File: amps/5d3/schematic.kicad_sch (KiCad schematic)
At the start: 43 parts, among them T2 PP : 8

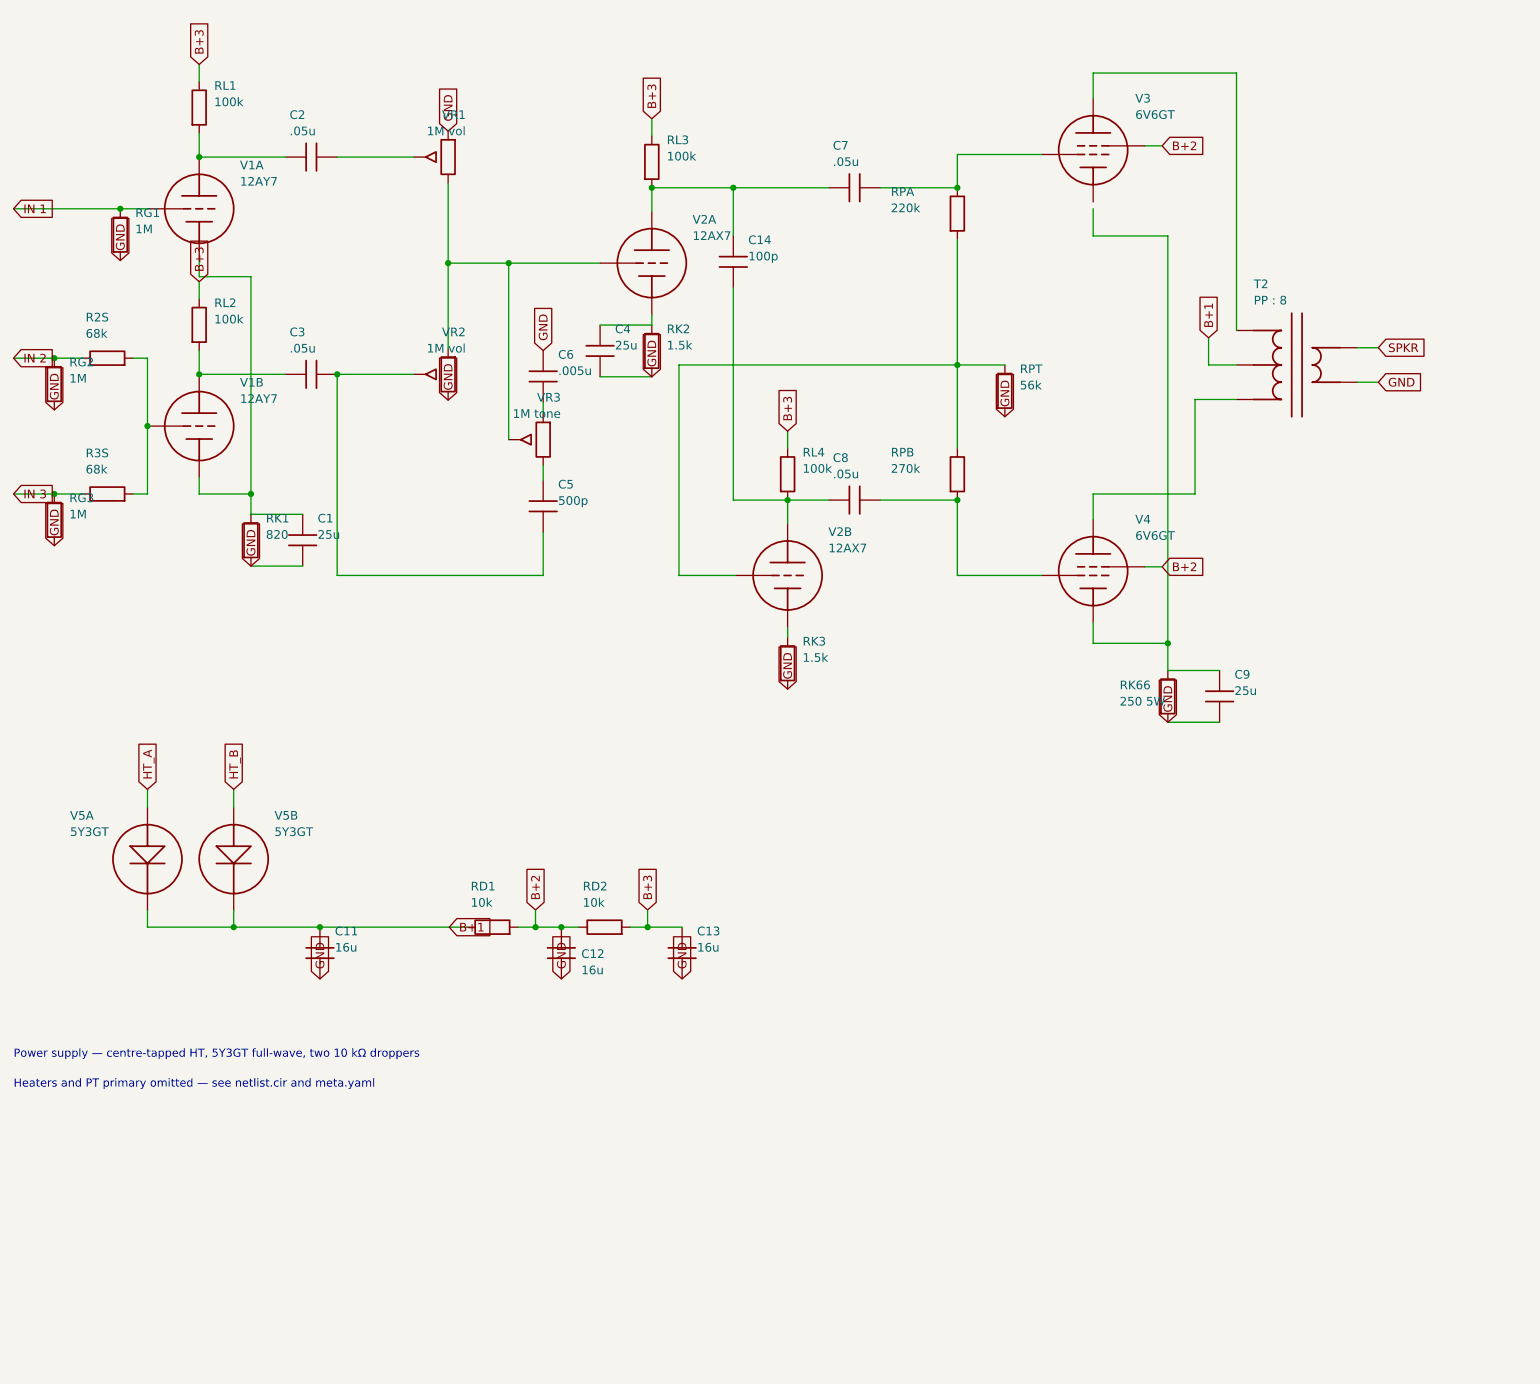
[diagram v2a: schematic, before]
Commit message: Fix: rotated global labels lettered their net names outside the flag
Every global label this pipeline emitted carried (justify left) regardless of
rotation. KiCanvas — like KiCad — draws label text horizontally at 0/180 and
vertically at 90/270 and reads WHICH SIDE of the anchor it letters on from the
justification, so at 180 and 270 the name printed outside an empty flag
outline, struck through by the very wire it names: 219 labels at 180 deg
(including the input-jack flags at top-left of nearly every sheet, the first
glyphs a visitor reads) and 792 GND/rail flags at 270 whose names squeezed at
the flag mouth instead of lettering down the body. The library already
compensated rotation for property text (`pa`); this mirrors that logic for
global labels: justify right at 180/270, left at 0/90.

check_schematics gains the geometry clause whose absence let all 1011
instances through a "no lettering through circuitry" pass: it modelled the
flag box but never the label TEXT, so a name rendered on the wrong side was
invisible to it. The gate now proves justification compensates rotation on
every global label.

Two more things this exposed, fixed in the same engine pass:

- Placement now measures with the renderer's own Newstroke advance table
  (extracted from the vendored kicanvas.js) instead of a flat 0.68-em prose
  average that under-read part lettering by a quarter — the mechanism behind
  every "metered clean, printed through its neighbour" incident. The GATE
  deliberately keeps the coarse ruler: re-ruling it with renderer truth was
  tried and red-flagged 28 of 34 sheets over abutments three visual passes
  had already judged sub-visual (the two-rulers note in schematic_lib.py).
- place_captions' escape ladder runs further, because a banner caption
  measured truly is half again wider than the old estimate believed.

All 34 schematics regenerated; full gate suite green.

🤖 Generated with [Claude Code](https://claude.com/claude-code)

Co-Authored-By: Claude Fable 5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
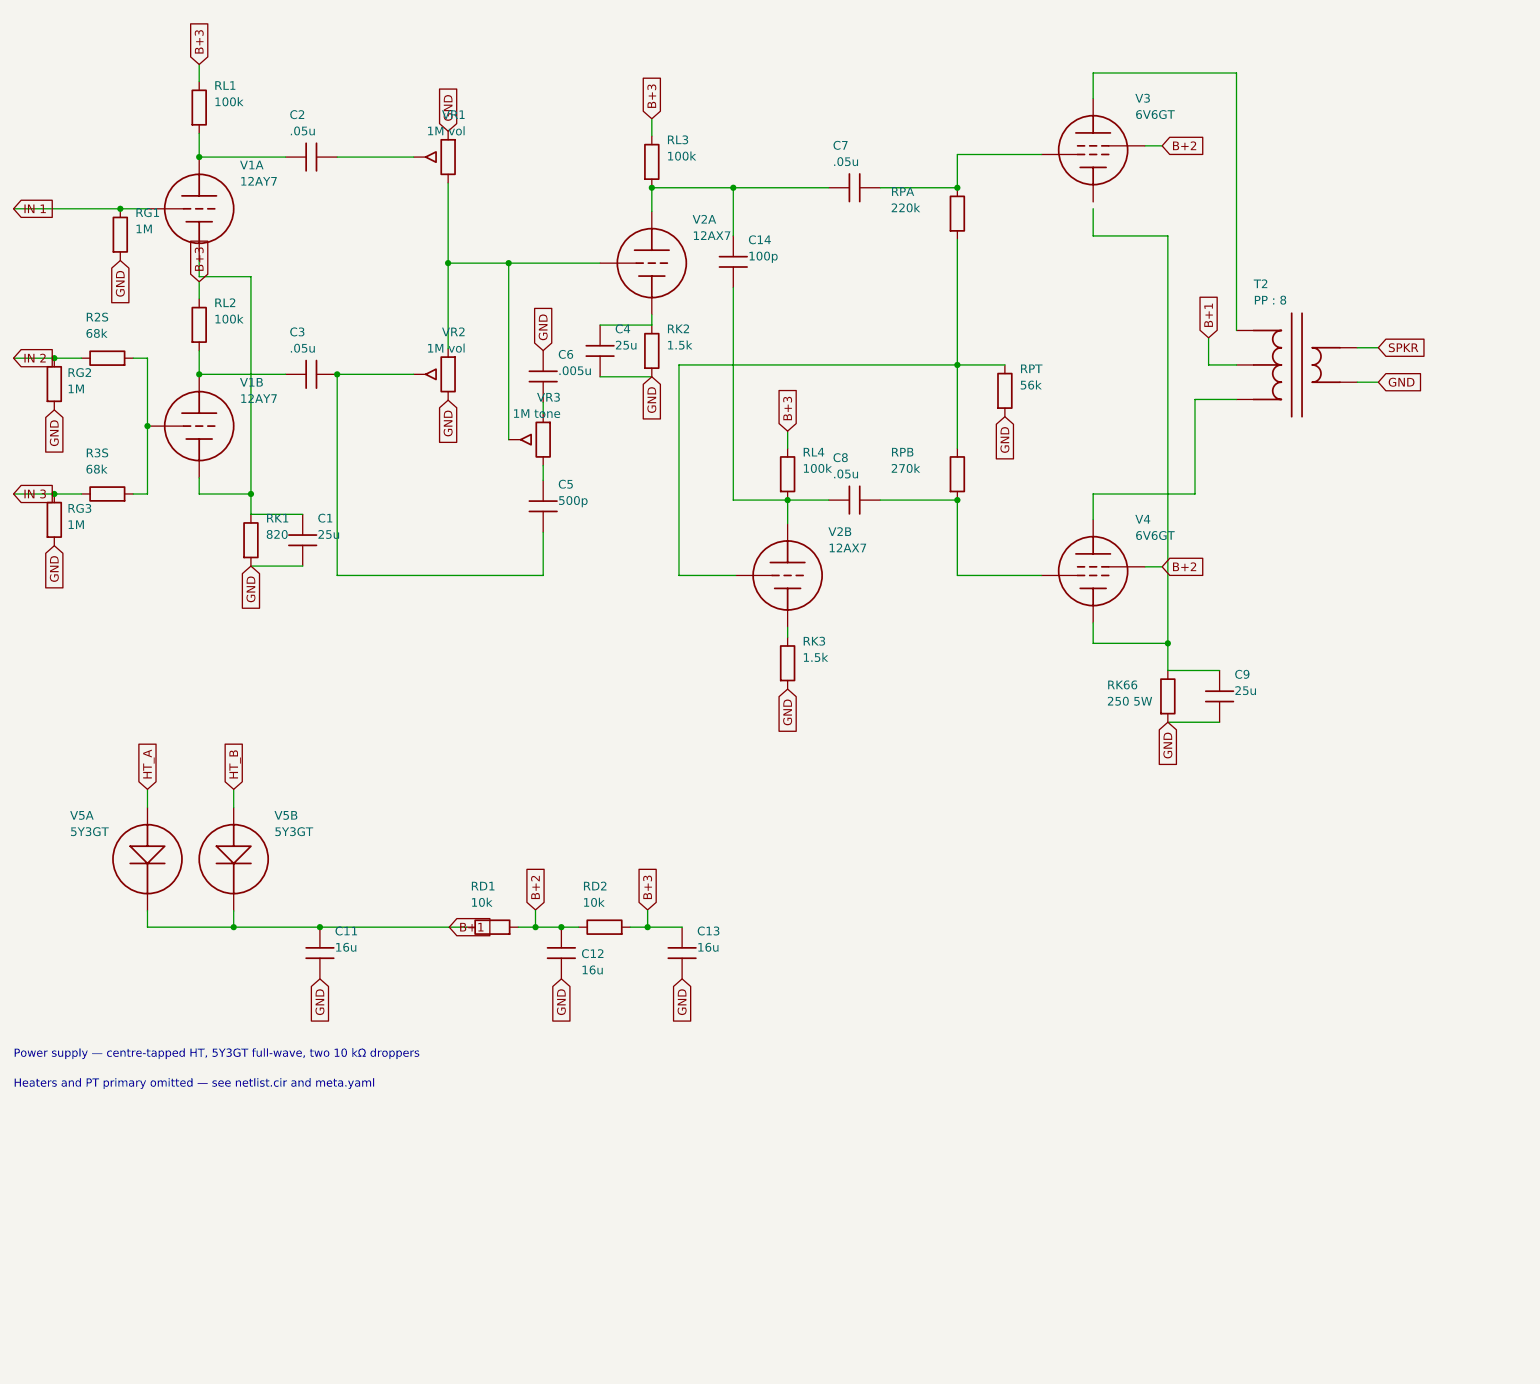
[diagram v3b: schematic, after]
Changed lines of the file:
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@@
     (property "Value" "1M" (at 30.62 41.288 0) (effects (font (size 1.27 1.27)) (justify left))))
   (global_label "GND" (shape input) (at 28.42 45.898 270)
-    (effects (font (size 1.27 1.27)) (justify left)))
+    (effects (font (size 1.27 1.27)) (justify right)))
   (wire (pts (xy 28.42 38.278) (xy 32.42 38.278))
     (stroke (width 0) (type default)))
@@
   (symbol (lib_id "cx:R") (at 18.7 64.088 0) (unit 1)
     (in_bom yes) (on_board yes)
-    (property "Reference" "RG2" (at 20.9 60.888 0) (effects (font (size 1.27 1.27)) (justify left)))
-    (property "Value" "1M" (at 20.9 63.288 0) (effects (font (size 1.27 1.27)) (justify left))))
+    (property "Reference" "RG2" (at 20.616 62.448 0) (effects (font (size 1.27 1.27)) (justify left)))
+    (property "Value" "1M" (at 20.616 64.848 0) (effects (font (size 1.27 1.27)) (justify left))))
   (global_label "GND" (shape input) (at 18.7 67.898 270)
-    (effects (font (size 1.27 1.27)) (justify left)))
+    (effects (font (size 1.27 1.27)) (justify right)))
   (symbol (lib_id "cx:R") (at 26.51 60.278 90) (unit 1)
     (in_bom yes) (on_board yes)
@@
   (symbol (lib_id "cx:R") (at 18.7 84.088 0) (unit 1)
     (in_bom yes) (on_board yes)
-    (property "Reference" "RG3" (at 20.9 80.888 0) (effects (font (size 1.27 1.27)) (justify left)))
-    (property "Value" "1M" (at 20.9 83.288 0) (effects (font (size 1.27 1.27)) (justify left))))
+    (property "Reference" "RG3" (at 20.616 82.448 0) (effects (font (size 1.27 1.27)) (justify left)))
+    (property "Value" "1M" (at 20.616 84.848 0) (effects (font (size 1.27 1.27)) (justify left))))
   (global_label "GND" (shape input) (at 18.7 87.898 270)
-    (effects (font (size 1.27 1.27)) (justify left)))
+    (effects (font (size 1.27 1.27)) (justify right)))
   (symbol (lib_id "cx:R") (at 26.51 80.278 90) (unit 1)
     (in_bom yes) (on_board yes)
@@
     (stroke (width 0) (type default)))
   (global_label "GND" (shape input) (at 47.66 90.898 270)
-    (effects (font (size 1.27 1.27)) (justify left)))
+    (effects (font (size 1.27 1.27)) (justify right)))
   (wire (pts (xy 40.04 30.658) (xy 52.74 30.658))
     (stroke (width 0) (type default)))
@@
     (property "Value" "1M vol" (at 79.3 58.858 0) (effects (font (size 1.27 1.27)) (justify left))))
   (global_label "GND" (shape input) (at 76.7 66.468 270)
-    (effects (font (size 1.27 1.27)) (justify left)))
+    (effects (font (size 1.27 1.27)) (justify right)))
   (wire (pts (xy 76.7 58.848) (xy 76.7 46.278))
     (stroke (width 0) (type default)))
@@
     (stroke (width 0) (type default)))
   (global_label "GND" (shape input) (at 106.7 63.018 270)
-    (effects (font (size 1.27 1.27)) (justify left)))
+    (effects (font (size 1.27 1.27)) (justify right)))
   (symbol (lib_id "cx:TRIODE") (at 126.7 92.278 0) (unit 1)
     (in_bom yes) (on_board yes)
@@
     (property "Value" "1.5k" (at 128.9 104.408 0) (effects (font (size 1.27 1.27)) (justify left))))
   (global_label "GND" (shape input) (at 126.7 109.018 270)
-    (effects (font (size 1.27 1.27)) (justify left)))
+    (effects (font (size 1.27 1.27)) (justify right)))
   (junction (at 106.7 35.178) (diameter 0) (color 0 0 0 0))
   (wire (pts (xy 106.7 35.178) (xy 132.75 35.178))
@@
     (property "Value" "56k" (at 160.9 64.288 0) (effects (font (size 1.27 1.27)) (justify left))))
   (global_label "GND" (shape input) (at 158.7 68.898 270)
-    (effects (font (size 1.27 1.27)) (justify left)))
+    (effects (font (size 1.27 1.27)) (justify right)))
   (wire (pts (xy 151.7 61.278) (xy 110.7 61.278))
     (stroke (width 0) (type default)))
@@
   (symbol (lib_id "cx:R") (at 182.7 110.088 0) (unit 1)
     (in_bom yes) (on_board yes)
-    (property "Reference" "RK66" (at 175.602 108.448 0) (effects (font (size 1.27 1.27)) (justify left)))
-    (property "Value" "250 5W" (at 175.602 110.848 0) (effects (font (size 1.27 1.27)) (justify left))))
+    (property "Reference" "RK66" (at 173.734 108.448 0) (effects (font (size 1.27 1.27)) (justify left)))
+    (property "Value" "250 5W" (at 173.734 110.848 0) (effects (font (size 1.27 1.27)) (justify left))))
   (symbol (lib_id "cx:C") (at 190.32 110.088 0) (unit 1)
     (in_bom yes) (on_board yes)
@@
     (stroke (width 0) (type default)))
   (global_label "GND" (shape input) (at 182.7 113.898 270)
-    (effects (font (size 1.27 1.27)) (justify left)))
+    (effects (font (size 1.27 1.27)) (justify right)))
   (symbol (lib_id "cx:OT_PP") (at 201.7 61.278 0) (unit 1)
     (in_bom yes) (on_board yes)
@@
     (property "Value" "16u" (at 60.02 147.088 0) (effects (font (size 1.27 1.27)) (justify left))))
   (global_label "GND" (shape input) (at 57.82 151.698 270)
-    (effects (font (size 1.27 1.27)) (justify left)))
+    (effects (font (size 1.27 1.27)) (justify right)))
   (global_label "B+1" (shape input) (at 76.87 144.078 0)
     (effects (font (size 1.27 1.27)) (justify left)))
@@
     (property "Value" "16u" (at 96.312 150.426 0) (effects (font (size 1.27 1.27)) (justify left))))
   (global_label "GND" (shape input) (at 93.38 151.698 270)
-    (effects (font (size 1.27 1.27)) (justify left)))
+    (effects (font (size 1.27 1.27)) (justify right)))
   (symbol (lib_id "cx:R") (at 99.73 144.078 90) (unit 1)
     (in_bom yes) (on_board yes)
@@
     (property "Value" "16u" (at 113.36 147.088 0) (effects (font (size 1.27 1.27)) (justify left))))
   (global_label "GND" (shape input) (at 111.16 151.698 270)
-    (effects (font (size 1.27 1.27)) (justify left)))
+    (effects (font (size 1.27 1.27)) (justify right)))
   (text "Power supply — centre-tapped HT, 5Y3GT full-wave, two 10 kΩ droppers" (at 12.7 162.856 0)
     (effects (font (size 1.2 1.2)) (justify left)))
